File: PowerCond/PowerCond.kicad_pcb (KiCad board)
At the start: 2 copper layers, 208.3 x 48.3 mm, 62 parts, among them J1 Conn_01x02, J10 Conn_01x01, J11 Conn_01x01, J12 Conn_01x01, J2 Conn_01x02, J3 Conn_01x02, J4 Conn_01x02, J5 Conn_01x02, J6 Conn_01x02, J7 Conn_01x02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

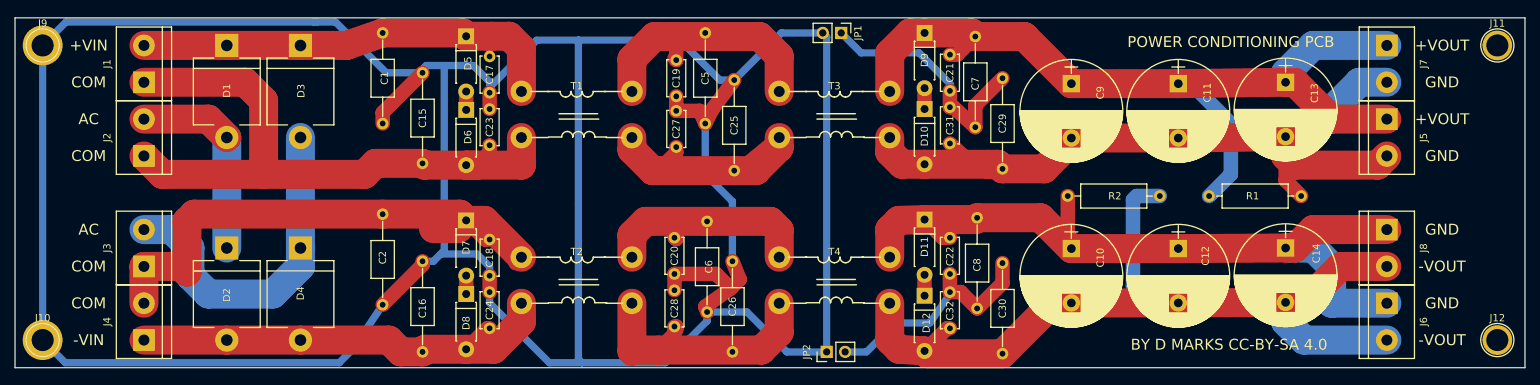
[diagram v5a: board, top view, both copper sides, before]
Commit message: Added option for spade terminal power connections
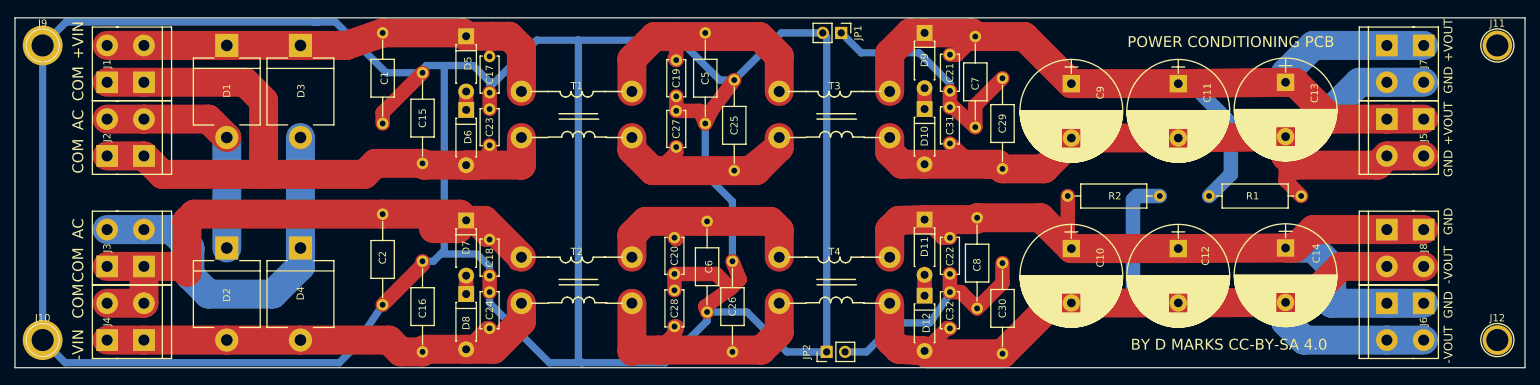
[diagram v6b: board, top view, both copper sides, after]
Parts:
- J1, J2, J3, J4, J5, J6, J7, J8: footprint Connectors_Terminal_Blocks:TerminalBlock_bornier-2_P5.08mm -> PowerCond:TerminalBlock_bornier-2_P5.08mm_with_spade
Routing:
- net Net-(C11-Pad2): track 110.7 -> 120.9 mm
- net Net-(C11-Pad1): track 122.1 -> 132.3 mm
- net Net-(C10-Pad2): track 124.9 -> 135.0 mm
- net Net-(C10-Pad1): track 107.9 -> 118.1 mm
- net Net-(C18-Pad1): track 77.8 -> 88.0 mm
- net Net-(C15-Pad2): track 90.3 -> 100.5 mm
- net Net-(D1-Pad2): track 27.7 -> 32.8 mm
- net Net-(C1-Pad1): track 63.4 -> 68.5 mm
- net Net-(D3-Pad2): track 46.9 -> 51.9 mm
- net Net-(C16-Pad2): track 62.2 -> 67.3 mm
